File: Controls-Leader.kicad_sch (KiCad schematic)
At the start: 48 parts, among them J1 ExtraADCs, J13 UART_TP, J15 Conn_02x03_Odd_Even, J2 UART_TP, J25 UART_TP, J3 ExtraGPIO_Conn, J8 SWD, SW10 RESET, U7 STM32F413RHTx, Y1 Crystal

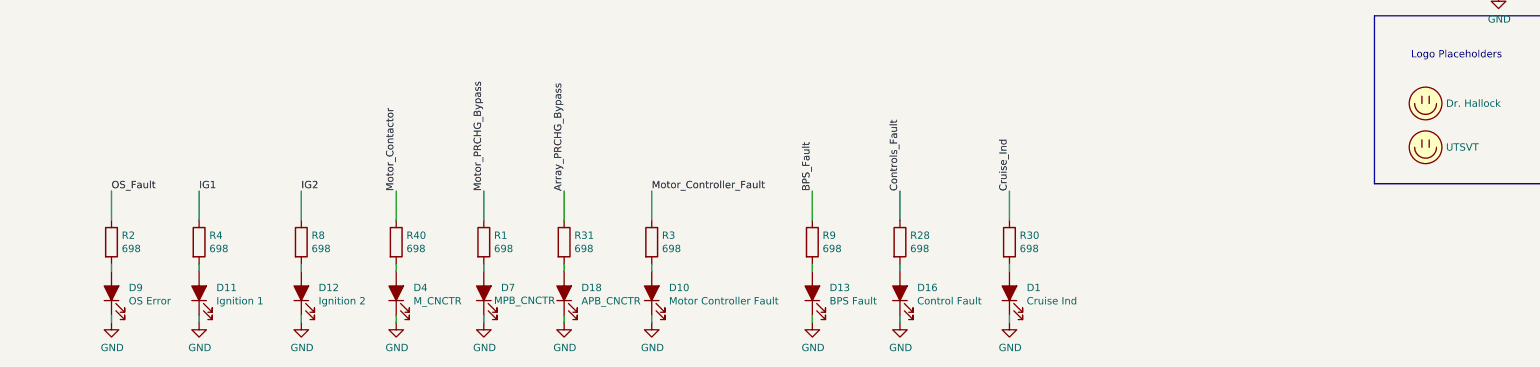
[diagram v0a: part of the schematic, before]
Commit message: Updated some symbols to use common libraries (and get rid of warnings.
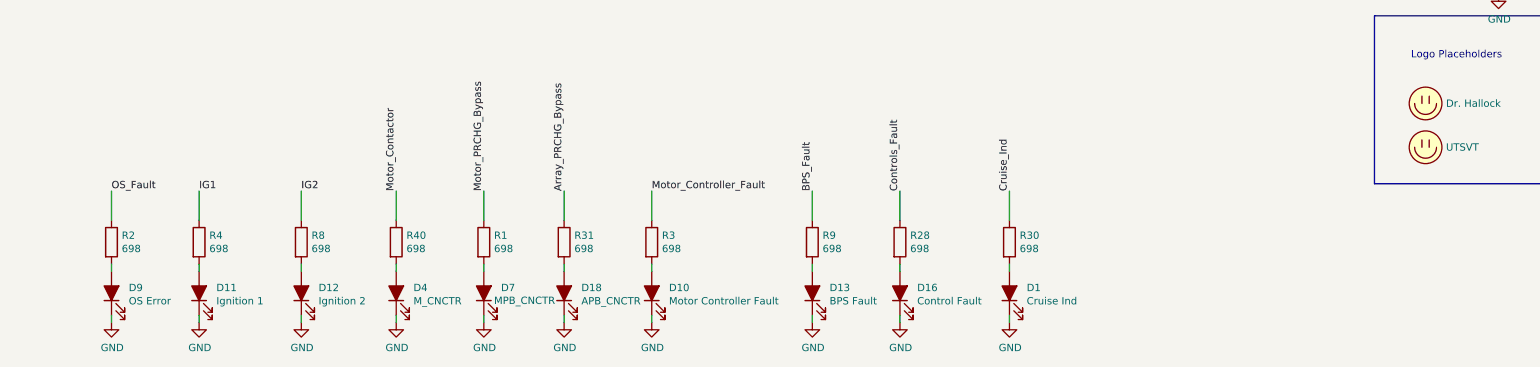
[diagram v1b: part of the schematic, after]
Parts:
- D1, D10, D11, D12, D13, D16, D18, D4, D7, D9: symbol Device:LED_ALT -> Device:LED_Filled
- LOGO1, LOGO2: symbol Dashboard-rescue:Logo_Placeholder-utsvt-misc -> utsvt-misc:Logo_Placeholder
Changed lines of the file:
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@@
 	)
 	(symbol
-		(lib_id "Dashboard-rescue:Logo_Placeholder-utsvt-misc")
+		(lib_id "utsvt-misc:Logo_Placeholder")
 		(at 304.8 241.3 0)
 		(unit 1)
@@
 	)
 	(symbol
-		(lib_id "Dashboard-rescue:Logo_Placeholder-utsvt-misc")
+		(lib_id "utsvt-misc:Logo_Placeholder")
 		(at 304.8 233.68 0)
 		(unit 1)
@@
 	)
 	(symbol
-		(lib_id "Device:LED_ALT")
+		(lib_id "Device:LED_Filled")
 		(at 91.44 266.7 90)
 		(unit 1)
@@
 	)
 	(symbol
-		(lib_id "Device:LED_ALT")
+		(lib_id "Device:LED_Filled")
 		(at 125.73 266.7 90)
 		(unit 1)
@@
 	)
 	(symbol
-		(lib_id "Device:LED_ALT")
+		(lib_id "Device:LED_Filled")
 		(at 76.2 266.7 90)
 		(unit 1)
@@
 	)
 	(symbol
-		(lib_id "Device:LED_ALT")
+		(lib_id "Device:LED_Filled")
 		(at 198.12 266.7 90)
 		(unit 1)
@@
 	)
 	(symbol
-		(lib_id "Device:LED_ALT")
+		(lib_id "Device:LED_Filled")
 		(at 213.36 266.7 90)
 		(unit 1)
@@
 	)
 	(symbol
-		(lib_id "Device:LED_ALT")
+		(lib_id "Device:LED_Filled")
 		(at 232.41 266.7 90)
 		(unit 1)
@@
 	)
 	(symbol
-		(lib_id "Device:LED_ALT")
+		(lib_id "Device:LED_Filled")
 		(at 109.22 266.7 90)
 		(unit 1)
@@
 	)
 	(symbol
-		(lib_id "Device:LED_ALT")
+		(lib_id "Device:LED_Filled")
 		(at 154.94 266.7 90)
 		(unit 1)
@@
 	)
 	(symbol
-		(lib_id "Device:LED_ALT")
+		(lib_id "Device:LED_Filled")
 		(at 170.18 266.7 90)
 		(unit 1)
@@
 	)
 	(symbol
-		(lib_id "Device:LED_ALT")
+		(lib_id "Device:LED_Filled")
 		(at 140.97 266.7 90)
 		(unit 1)

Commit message: Updated comments.
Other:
- company: UTSVT -> LHRS
- title: Dashboard -> Controls Leader
- moved on the sheet: J13
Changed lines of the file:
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@@
 	(paper "A3")
 	(title_block
-		(title "Dashboard")
-		(date "2020-06-06")
-		(rev "2.0")
-		(company "UTSVT")
-		(comment 1 "Author: Chase Block")
+		(title "Controls Leader")
+		(date "2025-01-18")
+		(rev "2.5")
+		(company "LHRS")
+		(comment 1 "Authors: Krish Parikh, Madeleine Lee")
 	)
 	(junction
@@
 		)
 	)
-	(polyline
-		(pts
-			(xy 327.66 218.44) (xy 327.66 247.65)
-		)
-		(stroke
-			(width 0)
-			(type default)
-		)
-	)
 	(wire
 		(pts
@@
 	(wire
 		(pts
-			(xy 318.77 212.09) (xy 307.34 212.09)
+			(xy 336.55 205.74) (xy 325.12 205.74)
 		)
 		(stroke
@@
 	(wire
 		(pts
-			(xy 318.77 209.55) (xy 307.34 209.55)
+			(xy 336.55 203.2) (xy 325.12 203.2)
 		)
 		(stroke
@@
 	(wire
 		(pts
-			(xy 317.5 214.63) (xy 317.5 207.01)
+			(xy 335.28 208.28) (xy 335.28 200.66)
 		)
 		(stroke
@@
 	(wire
 		(pts
-			(xy 317.5 207.01) (xy 318.77 207.01)
+			(xy 335.28 200.66) (xy 336.55 200.66)
 		)
 		(stroke
@@
 	)
 	(label "UART3_Rx"
-		(at 307.34 209.55 0)
+		(at 325.12 203.2 0)
 		(fields_autoplaced yes)
 		(effects
@@
 	)
 	(label "UART3_Tx"
-		(at 307.34 212.09 0)
+		(at 325.12 205.74 0)
 		(fields_autoplaced yes)
 		(effects
@@
 	(symbol
 		(lib_id "power:GND")
-		(at 317.5 214.63 0)
+		(at 335.28 208.28 0)
 		(unit 1)
 		(exclude_from_sim no)
@@
 		(dnp no)
 		(property "Reference" "#PWR033"
-			(at 317.5 220.98 0)
+			(at 335.28 214.63 0)
 			(effects
 				(font
@@
 		)
 		(property "Value" "GND"
-			(at 317.627 219.0242 0)
+			(at 335.407 212.6742 0)
 			(effects
 				(font
@@
 		)
 		(property "Footprint" ""
-			(at 317.5 214.63 0)
+			(at 335.28 208.28 0)
 			(effects
 				(font
@@
 		)
 		(property "Datasheet" ""
-			(at 317.5 214.63 0)
+			(at 335.28 208.28 0)
 			(effects
 				(font
@@
 		)
 		(property "Description" "Power symbol creates a global label with name \"GND\" , ground"
-			(at 317.5 214.63 0)
+			(at 335.28 208.28 0)
 			(effects
 				(font
@@
 	(symbol
 		(lib_id "Connector_Generic:Conn_01x03")
-		(at 323.85 209.55 0)
+		(at 341.63 203.2 0)
 		(unit 1)
 		(exclude_from_sim no)
@@
 		(dnp no)
 		(property "Reference" "J13"
-			(at 327.66 209.55 0)
+			(at 345.44 203.2 0)
 			(effects
 				(font
@@
 		)
 		(property "Value" "UART_TP"
-			(at 330.2 212.09 0)
+			(at 347.98 205.74 0)
 			(effects
 				(font
@@
 		)
 		(property "Footprint" "Connector_PinHeader_2.54mm:PinHeader_1x03_P2.54mm_Vertical"
-			(at 323.85 209.55 0)
+			(at 341.63 203.2 0)
 			(effects
 				(font
@@
 		)
 		(property "Datasheet" "~"
-			(at 323.85 209.55 0)
+			(at 341.63 203.2 0)
 			(effects
 				(font
@@
 		)
 		(property "Description" "Generic connector, single row, 01x03, script generated (kicad-library-utils/schlib/autogen/connector/)"
-			(at 323.85 209.55 0)
+			(at 341.63 203.2 0)
 			(effects
 				(font
@@
 		)
 		(property "Id" ""
-			(at 323.85 209.55 0)
+			(at 341.63 203.2 0)
 			(effects
 				(font
@@
 		)
 		(property "Vds" ""
-			(at 323.85 209.55 0)
+			(at 341.63 203.2 0)
 			(effects
 				(font

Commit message: Replaced unavailable parts
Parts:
- R1, R2, R28, R3, R30, R31, R4, R40, R8, R9: Mouser Part Number 71-CRCW0805698RFKEAC -> 652-CR0805FX-6980ELF; P/N (none) -> CR0805-FX-6980ELF

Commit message: Filled in part numbers, exported BOM and made Excel file for working with it.
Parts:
- C10, C13: P/N (none) -> GRM219R6YA475KA3D
- C11, C12, C14, C5, C6, C9: P/N (none) -> C0805C104M5R
- C7, C8: P/N (none) -> C0805C120K5HACTU
- H1, H2, H3, H4, J1: P/N (none) -> 436500315
- R18: P/N (none) -> CRCW080510K0FKEAC
- SW10: P/N (none) -> B3SL-1002P
- U7: P/N (none) -> STM32F413RHT6
- Y1: Mouser Part Number ABM3-8.000MHZ-D2Y-T -> (none); P/N (none) -> ABM3-8.000MHZ-D2Y-T
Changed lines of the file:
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@@
 			)
 		)
+		(property "P/N" "436500315"
+			(at 334.01 232.41 0)
+			(effects
+				(font
+					(size 1.27 1.27)
+				)
+				(hide yes)
+			)
+		)
 		(instances
 			(project "Controls-Leader"
@@
 			)
 		)
+		(property "P/N" "436500315"
+			(at 334.01 237.49 0)
+			(effects
+				(font
+					(size 1.27 1.27)
+				)
+				(hide yes)
+			)
+		)
 		(instances
 			(project "Controls-Leader"
@@
 			)
 		)
+		(property "P/N" "436500315"
+			(at 334.01 242.57 0)
+			(effects
+				(font
+					(size 1.27 1.27)
+				)
+				(hide yes)
+			)
+		)
 		(instances
 			(project "Controls-Leader"
@@
 			)
 		)
+		(property "P/N" "436500315"
+			(at 353.06 232.41 0)
+			(effects
+				(font
+					(size 1.27 1.27)
+				)
+				(hide yes)
+			)
+		)
 		(instances
 			(project "Controls-Leader"
@@
 			)
 		)
+		(property "P/N" "STM32F413RHT6"
+			(at 210.82 158.75 0)
+			(effects
+				(font
+					(size 1.27 1.27)
+				)
+				(hide yes)
+			)
+		)
 		(pin "1"
 		)
@@
 			)
 		)
+		(property "P/N" "CRCW080510K0FKEAC "
+			(at 173.99 114.3 0)
+			(effects
+				(font
+					(size 1.27 1.27)
+				)
+				(hide yes)
+			)
+		)
 		(pin "1"
 		)
@@
 			)
 		)
+		(property "P/N" "B3SL-1002P"
+			(at 153.67 110.49 0)
+			(effects
+				(font
+					(size 1.27 1.27)
+				)
+				(hide yes)
+			)
+		)
 		(pin "1"
 		)
@@
 			)
 		)
+		(property "P/N" "C0805C104M5R"
+			(at 167.64 109.22 0)
+			(effects
+				(font
+					(size 1.27 1.27)
+				)
+				(hide yes)
+			)
+		)
 		(pin "1"
 		)
@@
 			)
 		)
+		(property "P/N" "GRM219R6YA475KA3D"
+			(at 181.61 184.15 0)
+			(effects
+				(font
+					(size 1.27 1.27)
+				)
+				(hide yes)
+			)
+		)
 		(pin "1"
 		)
@@
 			)
 		)
-		(property "Mouser Part Number" "ABM3-8.000MHZ-D2Y-T"
+		(property "Mouser Part Number" ""
 			(at 180.34 129.54 0)
 			(effects
@@
 			)
 		)
+		(property "P/N" "ABM3-8.000MHZ-D2Y-T"
+			(at 180.34 129.54 0)
+			(effects
+				(font
+					(size 1.27 1.27)
+				)
+				(hide yes)
+			)
+		)
 		(pin "1"
 		)
@@
 			)
 		)
+		(property "P/N" "C0805C120K5HACTU"
+			(at 171.45 125.73 0)
+			(effects
+				(font
+					(size 1.27 1.27)
+				)
+				(hide yes)
+			)
+		)
 		(pin "1"
 		)
@@
 			)
 		)
+		(property "P/N" "C0805C120K5HACTU"
+			(at 171.45 133.35 0)
+			(effects
+				(font
+					(size 1.27 1.27)
+				)
+				(hide yes)
+			)
+		)
 		(pin "1"
 		)
@@
 			)
 		)
+		(property "P/N" "C0805C104M5R"
+			(at 170.18 67.31 0)
+			(effects
+				(font
+					(size 1.27 1.27)
+				)
+				(hide yes)
+			)
+		)
 		(pin "1"
 		)
@@
 			)
 		)
+		(property "P/N" "GRM219R6YA475KA3D"
+			(at 217.17 67.31 0)
+			(effects
+				(font
+					(size 1.27 1.27)
+				)
+				(hide yes)
+			)
+		)
 		(pin "1"
 		)
@@
 			)
 		)
+		(property "P/N" "C0805C104M5R"
+			(at 232.41 67.31 0)
+			(effects
+				(font
+					(size 1.27 1.27)
+				)
+				(hide yes)
+			)
+		)
 		(pin "1"
 		)
@@
 			)
 		)
+		(property "P/N" "C0805C104M5R"
+			(at 181.61 67.31 0)
+			(effects
+				(font
+					(size 1.27 1.27)
+				)
+				(hide yes)
+			)
+		)
 		(pin "1"
 		)
@@
 			)
 		)
+		(property "P/N" "C0805C104M5R"
+			(at 193.04 67.31 0)
+			(effects
+				(font
+					(size 1.27 1.27)
+				)
+				(hide yes)
+			)
+		)
 		(pin "1"
 		)
@@
 			)
 		)
+		(property "P/N" "C0805C104M5R"
+			(at 204.47 67.31 0)
+			(effects
+				(font
+					(size 1.27 1.27)
+				)
+				(hide yes)
+			)
+		)
 		(pin "1"
 		)
@@
 			(at 345.44 173.99 0)
 			(effects
+				(font
+					(size 1.27 1.27)
+				)
+				(hide yes)
+			)
+		)
+		(property "P/N" "436500315"
+			(at 345.44 173.99 0)
+			(effects

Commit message: Added names to board, update BOM.
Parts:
- H1, H2, H3, H4: P/N 436500315 -> (none)
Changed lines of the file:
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@@
 			)
 		)
-		(property "P/N" "436500315"
+		(property "P/N" ""
 			(at 334.01 232.41 0)
 			(effects
@@
 			)
 		)
-		(property "P/N" "436500315"
+		(property "P/N" ""
 			(at 334.01 237.49 0)
 			(effects
@@
 			)
 		)
-		(property "P/N" "436500315"
+		(property "P/N" ""
 			(at 334.01 242.57 0)
 			(effects
@@
 			)
 		)
-		(property "P/N" "436500315"
-			(at 353.06 232.41 0)
-			(effects
+		(property "P/N" ""
+			(at 353.06 232.41 0)
+			(effects

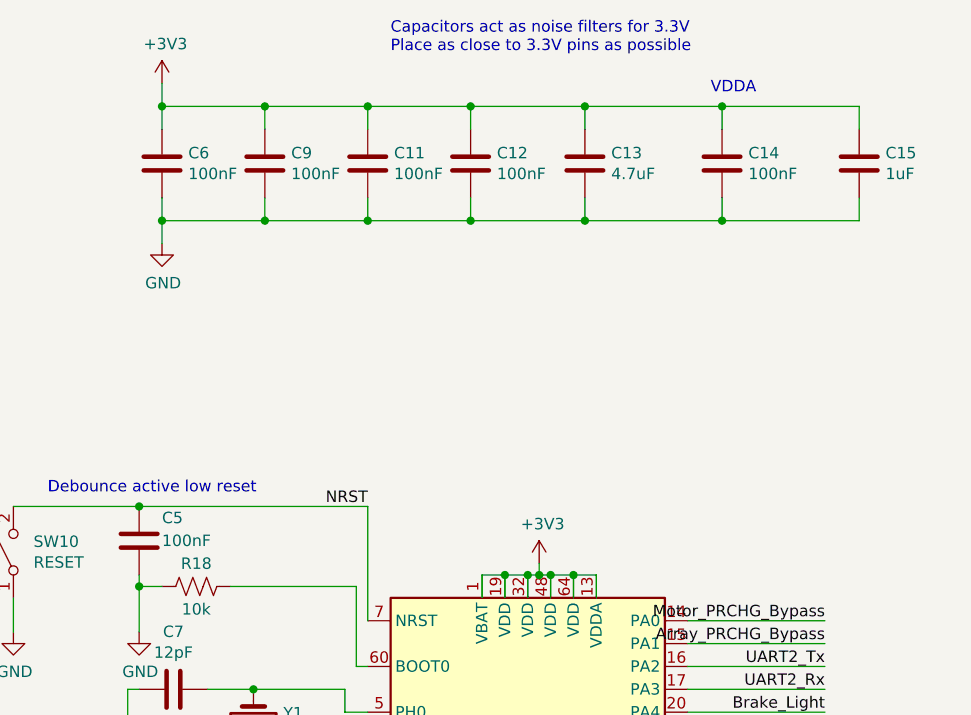
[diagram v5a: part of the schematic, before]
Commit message: Updated BOM a little (group parts better, usb pn was actually 1 number off).
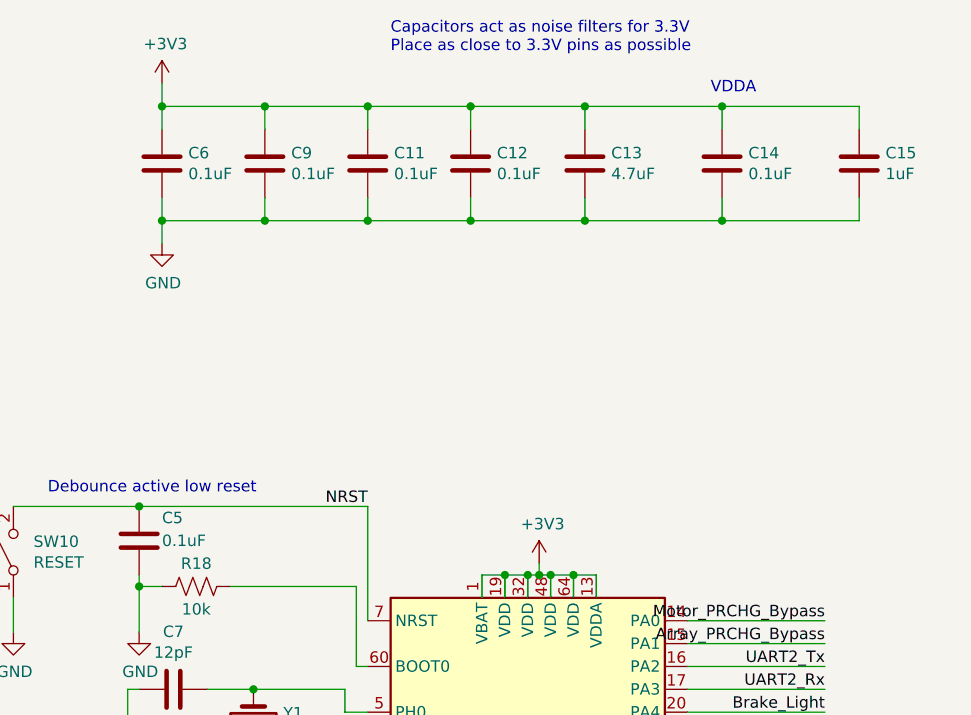
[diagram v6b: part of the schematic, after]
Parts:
- C11, C12, C14, C5, C6, C9: value 100nF -> 0.1uF
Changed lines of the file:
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@@
 			)
 		)
-		(property "Value" "100nF"
+		(property "Value" "0.1uF"
 			(at 170.18 109.22 0)
 			(effects
@@
 			)
 		)
-		(property "Value" "100nF"
+		(property "Value" "0.1uF"
 			(at 173.101 68.453 0)
 			(effects
@@
 			)
 		)
-		(property "Value" "100nF"
+		(property "Value" "0.1uF"
 			(at 235.331 68.453 0)
 			(effects
@@
 			)
 		)
-		(property "Value" "100nF"
+		(property "Value" "0.1uF"
 			(at 184.531 68.453 0)
 			(effects
@@
 			)
 		)
-		(property "Value" "100nF"
+		(property "Value" "0.1uF"
 			(at 195.961 68.453 0)
 			(effects
@@
 			)
 		)
-		(property "Value" "100nF"
+		(property "Value" "0.1uF"
 			(at 207.391 68.453 0)
 			(effects

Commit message: Added version update notes.
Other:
- note added: "Controls Leaderboard: Daybreak Rework 2025 An intermediate board between the 2022-2024 and 2024-2026 cars that merges the Daybreak Controls Leaderboard and Lighting Board. Created in conjunction with the new 2025 Controls Dashboard. See sub-sheets for additional revisions since last version."
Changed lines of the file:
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@@
+		)
+	)
+	(rectangle
+		(start 329.438 12.065)
+		(end 407.924 26.162)
+		(stroke
+			(width 0)
+			(type default)
+			(color 251 48 27 1)
+		)
+		(fill
+			(type none)
 		)
 	)
@@
 		)
 	)
+	(text "Controls Leaderboard: Daybreak Rework 2025\nAn intermediate board between the 2022-2024 and 2024-2026 cars\nthat merges the Daybreak Controls Leaderboard and Lighting Board.\nCreated in conjunction with the new 2025 Controls Dashboard.\nSee sub-sheets for additional revisions since last version."
+		(exclude_from_sim no)
+		(at 332.232 18.542 0)
+		(effects
+			(font
+				(size 1.27 1.27)
+				(color 205 56 62 1)
+			)
+			(justify left)
+		)
+	)

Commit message: Moved version update notes.
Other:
- note added: "Controls Leaderboard: Daybreak Rework 2025 - An intermediate board between the 2022-2024 and 2024-2026 cars that merges the Daybreak Controls Leaderboard and Lighting Board. - Created in conjunction with the new 2025 Controls Dashboard. - See sub-sheets for additional revisions since last version."
- note removed: "Controls Leaderboard: Daybreak Rework 2025 An intermediate board between the 2022-2024 and 2024-2026 cars that merges the Daybreak Controls Leaderboard and Lighting Board. Created in conjunction with the new 2025 Controls Dashboard. See sub-sheets for additional revisions since last version."
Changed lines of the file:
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@@
-		)
-	)
-	(rectangle
-		(start 329.438 12.065)
-		(end 407.924 26.162)
-		(stroke
-			(width 0)
-			(type default)
-			(color 251 48 27 1)
-		)
-		(fill
-			(type none)
 		)
 	)
@@
 		)
 	)
-	(text "Controls Leaderboard: Daybreak Rework 2025\nAn intermediate board between the 2022-2024 and 2024-2026 cars\nthat merges the Daybreak Controls Leaderboard and Lighting Board.\nCreated in conjunction with the new 2025 Controls Dashboard.\nSee sub-sheets for additional revisions since last version."
+	(text "Controls Leaderboard: Daybreak Rework 2025\n- An intermediate board between the 2022-2024 and 2024-2026 cars\n   that merges the Daybreak Controls Leaderboard and Lighting Board.\n- Created in conjunction with the new 2025 Controls Dashboard.\n- See sub-sheets for additional revisions since last version."
 		(exclude_from_sim no)
-		(at 332.232 18.542 0)
+		(at 300.736 257.81 0)
 		(effects
 			(font
-				(size 1.27 1.27)
-				(color 205 56 62 1)
+				(size 1.016 1.016)
+				(color 255 69 46 1)
 			)
 			(justify left)
